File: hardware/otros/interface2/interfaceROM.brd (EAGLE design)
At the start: 73.6 x 29.4 mm, 15 parts, among them IC1 74HC174N, IC4 AM29F040S

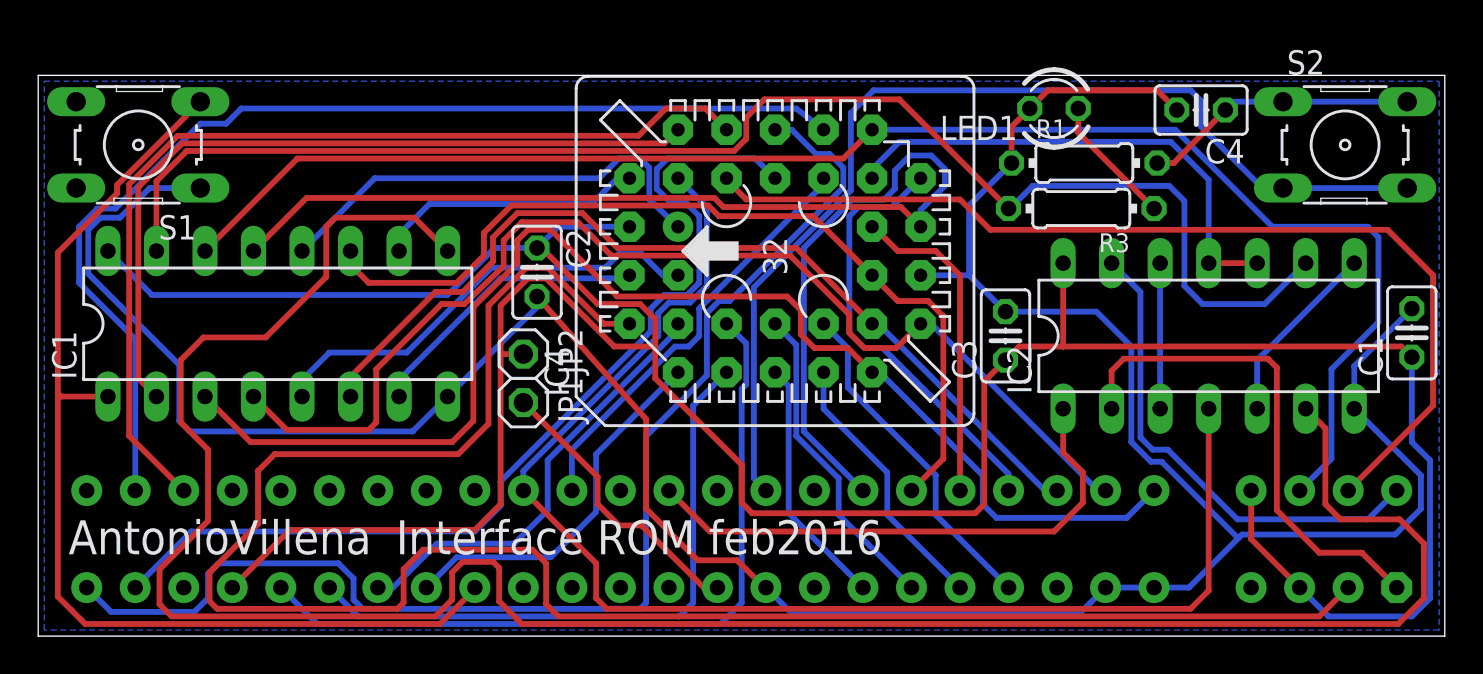
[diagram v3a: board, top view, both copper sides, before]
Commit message: Desconecto WR y lo pongo a VCC en iFrom
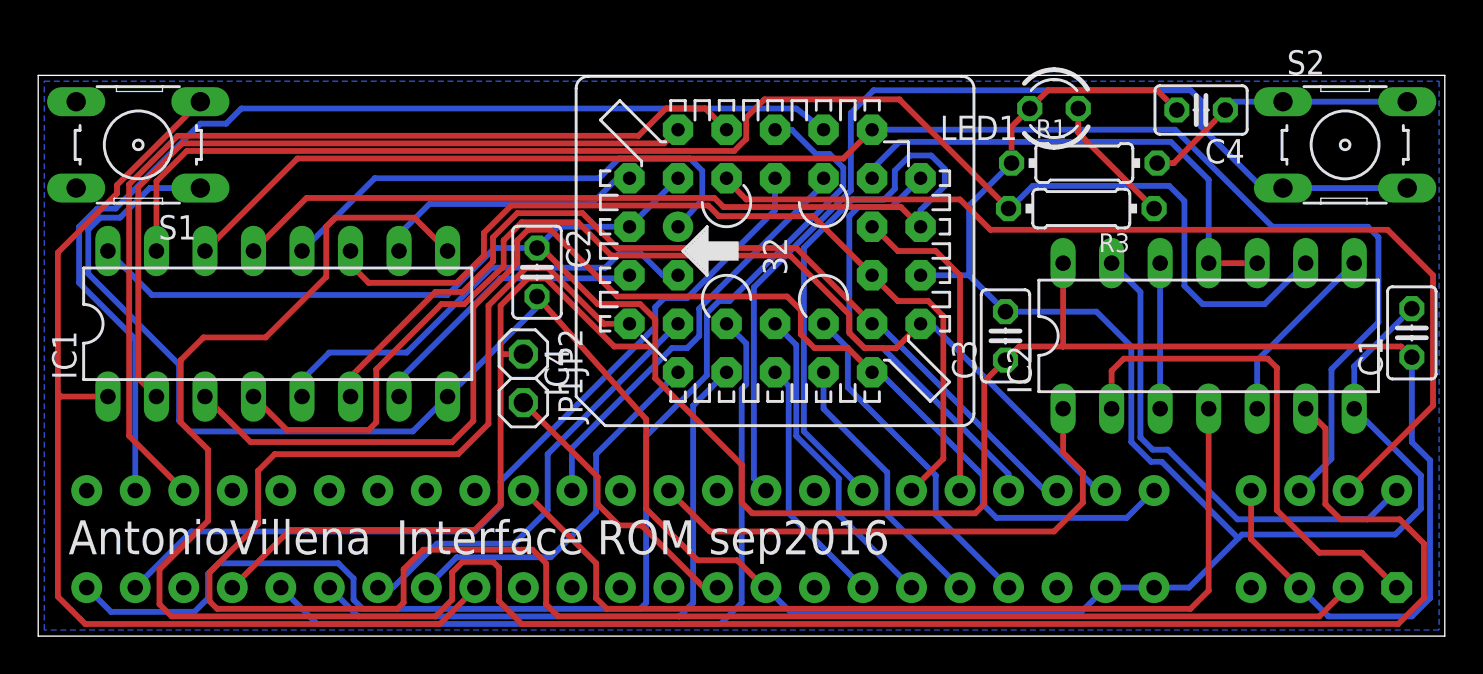
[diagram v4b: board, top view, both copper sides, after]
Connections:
- net VCC: now also IC4.31
- net WR: no longer IC4.31
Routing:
- net WR: track 71.0 -> 49.4 mm
- net A9: track 51.8 -> 44.7 mm
- net VCC: track 160.9 -> 164.5 mm
- net ROM18: track 24.1 -> 26.6 mm
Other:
- board text added: "Interface ROM sep2016"
- board text removed: "Interface ROM feb2016"
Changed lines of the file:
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@@
 <wire x1="73.64" y1="29.35625" x2="0" y2="29.35625" width="0" layer="46"/>
 <wire x1="0" y1="29.35625" x2="0" y2="0" width="0" layer="46"/>
-<text x="18.7325" y="4.28625" size="1.778" layer="21">Interface ROM feb2016</text>
+<text x="18.7325" y="4.28625" size="1.778" layer="21">Interface ROM sep2016</text>
 <text x="1.5875" y="4.28625" size="1.778" layer="21">AntonioVillena</text>
 </plain>
@@
 <wire x1="22.86" y1="5.476875" x2="24.209375" y2="6.82625" width="0.3048" layer="16"/>
 <wire x1="24.209375" y1="6.82625" x2="24.209375" y2="8.09625" width="0.3048" layer="16"/>
-<wire x1="24.209375" y1="8.09625" x2="32.0675" y2="15.954375" width="0.3048" layer="16"/>
-<wire x1="32.0675" y1="15.954375" x2="32.0675" y2="17.145" width="0.3048" layer="16"/>
-<wire x1="32.0675" y1="17.145" x2="32.781875" y2="17.859375" width="0.3048" layer="16"/>
-<wire x1="32.781875" y1="17.859375" x2="33.9725" y2="17.859375" width="0.3048" layer="16"/>
-<wire x1="33.9725" y1="17.859375" x2="34.6075" y2="18.494375" width="0.3048" layer="16"/>
-<wire x1="34.6075" y1="18.494375" x2="34.6075" y2="21.986875" width="0.3048" layer="16"/>
-<wire x1="34.6075" y1="21.986875" x2="33.893125" y2="22.70125" width="0.3048" layer="16"/>
-<wire x1="33.893125" y1="22.70125" x2="33.099375" y2="22.70125" width="0.3048" layer="16"/>
-<wire x1="33.099375" y1="22.70125" x2="32.385" y2="23.415625" width="0.3048" layer="16"/>
-<wire x1="32.385" y1="23.415625" x2="32.385" y2="24.4475" width="0.3048" layer="16"/>
-<wire x1="32.385" y1="24.4475" x2="32.940625" y2="25.003125" width="0.3048" layer="16"/>
-<wire x1="32.940625" y1="25.003125" x2="37.544375" y2="25.003125" width="0.3048" layer="16"/>
-<wire x1="37.544375" y1="25.003125" x2="38.57625" y2="23.97125" width="0.3048" layer="16"/>
+<wire x1="24.209375" y1="8.09625" x2="32.305625" y2="16.1925" width="0.3048" layer="16"/>
+<wire x1="32.305625" y1="16.1925" x2="32.305625" y2="17.224375" width="0.3048" layer="16"/>
+<wire x1="32.305625" y1="17.224375" x2="32.781875" y2="17.700625" width="0.3048" layer="16"/>
+<wire x1="32.781875" y1="17.700625" x2="33.9725" y2="17.700625" width="0.3048" layer="16"/>
+<wire x1="33.9725" y1="17.700625" x2="38.57625" y2="22.304375" width="0.3048" layer="16"/>
+<wire x1="38.57625" y1="22.304375" x2="38.57625" y2="23.97125" width="0.3048" layer="16"/>
 </signal>
 <signal name="A8">
@@
 <wire x1="63.5" y1="7.62" x2="63.5" y2="5.08" width="0.3048" layer="1"/>
 <wire x1="63.5" y1="5.08" x2="66.04" y2="2.54" width="0.3048" layer="1"/>
+<contactref element="IC4" pad="31"/>
+<wire x1="33.49625" y1="23.97125" x2="30.95625" y2="21.43125" width="0.3048" layer="16"/>
 </signal>
 <signal name="GND">
@@
 <wire x1="20.875625" y1="4.841875" x2="24.92375" y2="4.841875" width="0.3048" layer="16"/>
 <wire x1="24.92375" y1="4.841875" x2="26.67" y2="6.588125" width="0.3048" layer="16"/>
-<wire x1="26.67" y1="6.588125" x2="26.67" y2="9.2075" width="0.3048" layer="16"/>
-<wire x1="26.67" y1="9.2075" x2="33.49625" y2="16.03375" width="0.3048" layer="16"/>
-<wire x1="33.49625" y1="16.35125" x2="33.49625" y2="16.03375" width="0.3048" layer="16"/>
+<wire x1="26.67" y1="6.588125" x2="26.67" y2="9.525" width="0.3048" layer="16"/>
+<wire x1="26.67" y1="9.525" x2="33.49625" y2="16.35125" width="0.3048" layer="16"/>
 </signal>
 <signal name="A7">
@@
 <contactref element="U$3" pad="B18"/>
 <contactref element="IC4" pad="24"/>
-<wire x1="27.94" y1="7.62" x2="27.94" y2="9.763125" width="0.3048" layer="16"/>
-<wire x1="27.94" y1="9.763125" x2="33.3375" y2="15.160625" width="0.3048" layer="16"/>
-<wire x1="33.3375" y1="15.160625" x2="34.051875" y2="15.160625" width="0.3048" layer="16"/>
-<wire x1="34.051875" y1="15.160625" x2="34.6075" y2="15.71625" width="0.3048" layer="16"/>
+<wire x1="27.94" y1="7.62" x2="27.94" y2="9.8425" width="0.3048" layer="16"/>
+<wire x1="27.94" y1="9.8425" x2="33.17875" y2="15.08125" width="0.3048" layer="16"/>
+<wire x1="33.17875" y1="15.08125" x2="33.9725" y2="15.08125" width="0.3048" layer="16"/>
+<wire x1="33.9725" y1="15.08125" x2="34.6075" y2="15.71625" width="0.3048" layer="16"/>
 <wire x1="34.6075" y1="15.71625" x2="34.6075" y2="17.145" width="0.3048" layer="16"/>
 <wire x1="34.6075" y1="17.145" x2="41.11625" y2="23.65375" width="0.3048" layer="16"/>
@@
 <signal name="WR">
 <contactref element="U$3" pad="B19"/>
-<contactref element="IC4" pad="31"/>
 <contactref element="IC2" pad="4"/>
-<wire x1="33.02" y1="17.4625" x2="34.13125" y2="17.4625" width="0.3048" layer="16"/>
-<wire x1="34.13125" y1="17.4625" x2="35.004375" y2="18.335625" width="0.3048" layer="16"/>
-<wire x1="35.004375" y1="18.335625" x2="35.004375" y2="22.463125" width="0.3048" layer="16"/>
-<wire x1="35.004375" y1="22.463125" x2="33.49625" y2="23.97125" width="0.3048" layer="16"/>
-<wire x1="25.4" y1="7.62" x2="25.4" y2="8.651875" width="0.3048" layer="16"/>
-<wire x1="25.4" y1="8.651875" x2="32.464375" y2="15.71625" width="0.3048" layer="16"/>
-<wire x1="32.464375" y1="15.71625" x2="32.464375" y2="16.906875" width="0.3048" layer="16"/>
-<wire x1="32.464375" y1="16.906875" x2="33.02" y2="17.4625" width="0.3048" layer="16"/>
 <wire x1="61.2775" y1="11.90625" x2="61.2775" y2="2.38125" width="0.3048" layer="1"/>
 <wire x1="25.4" y1="7.62" x2="29.21" y2="3.81" width="0.3048" layer="1"/>
@@
 <contactref element="IC1" pad="12"/>
 <wire x1="29.36875" y1="23.97125" x2="30.400625" y2="25.003125" width="0.3048" layer="16"/>
-<wire x1="30.400625" y1="25.003125" x2="31.511875" y2="25.003125" width="0.3048" layer="16"/>
-<wire x1="31.511875" y1="25.003125" x2="31.988125" y2="24.526875" width="0.3048" layer="16"/>
-<wire x1="31.988125" y1="24.526875" x2="31.988125" y2="22.86" width="0.3048" layer="16"/>
-<wire x1="31.988125" y1="22.86" x2="33.49625" y2="21.43125" width="0.3048" layer="16"/>
+<wire x1="30.400625" y1="25.003125" x2="34.13125" y2="25.003125" width="0.3048" layer="16"/>
+<wire x1="34.13125" y1="25.003125" x2="34.76625" y2="24.368125" width="0.3048" layer="16"/>
+<wire x1="34.76625" y1="24.368125" x2="34.76625" y2="22.86" width="0.3048" layer="16"/>
+<wire x1="34.76625" y1="22.86" x2="33.49625" y2="21.43125" width="0.3048" layer="16"/>
 <wire x1="29.36875" y1="23.97125" x2="17.62125" y2="23.97125" width="0.3048" layer="16"/>
 <wire x1="17.62125" y1="23.97125" x2="13.81125" y2="20.16125" width="0.3048" layer="16"/>
